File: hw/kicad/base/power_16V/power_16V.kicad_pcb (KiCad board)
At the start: 2 copper layers, 45 x 45 mm, 33 parts, among them J1 USB_B_Micro, J3 TOP, J4 BUTTOM, U1 LM2596S-5, U2 LM1117MP-3.3, U3 CP2104

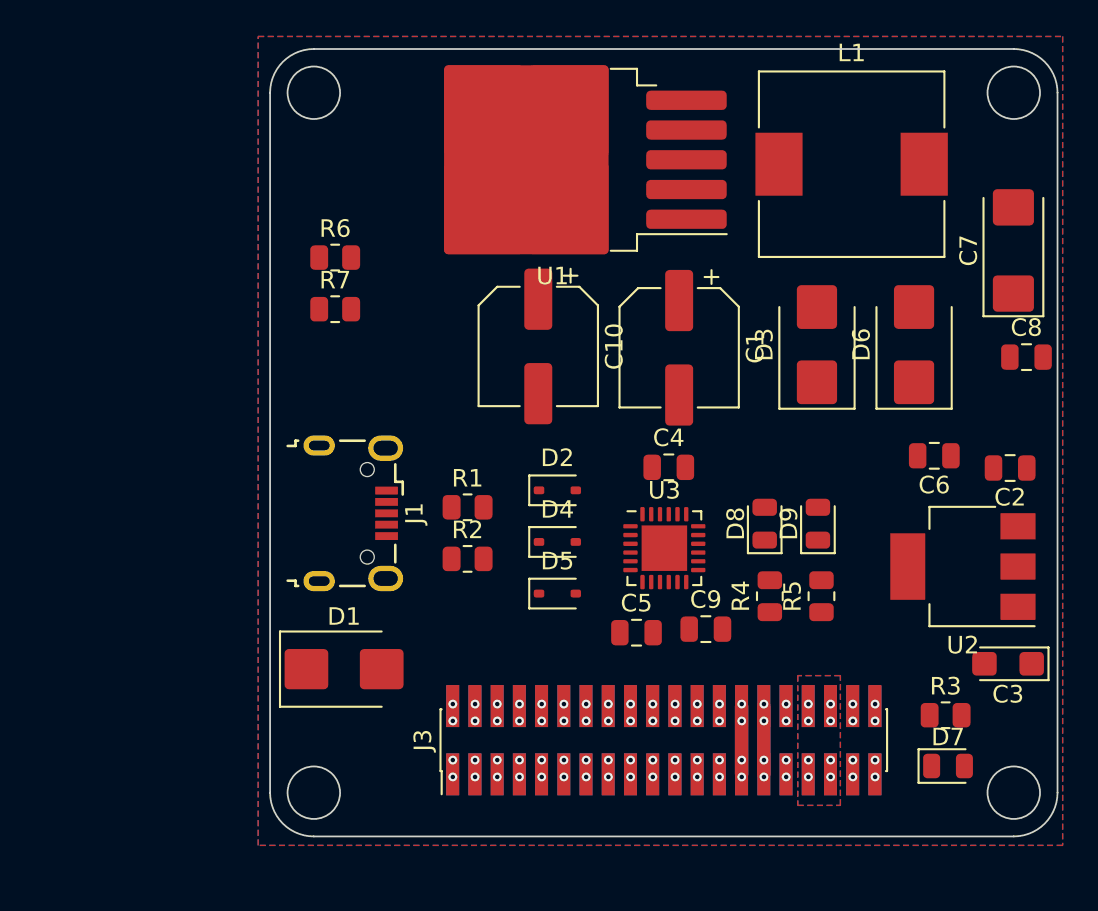
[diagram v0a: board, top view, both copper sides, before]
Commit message: 尽力改成40mmx40mm
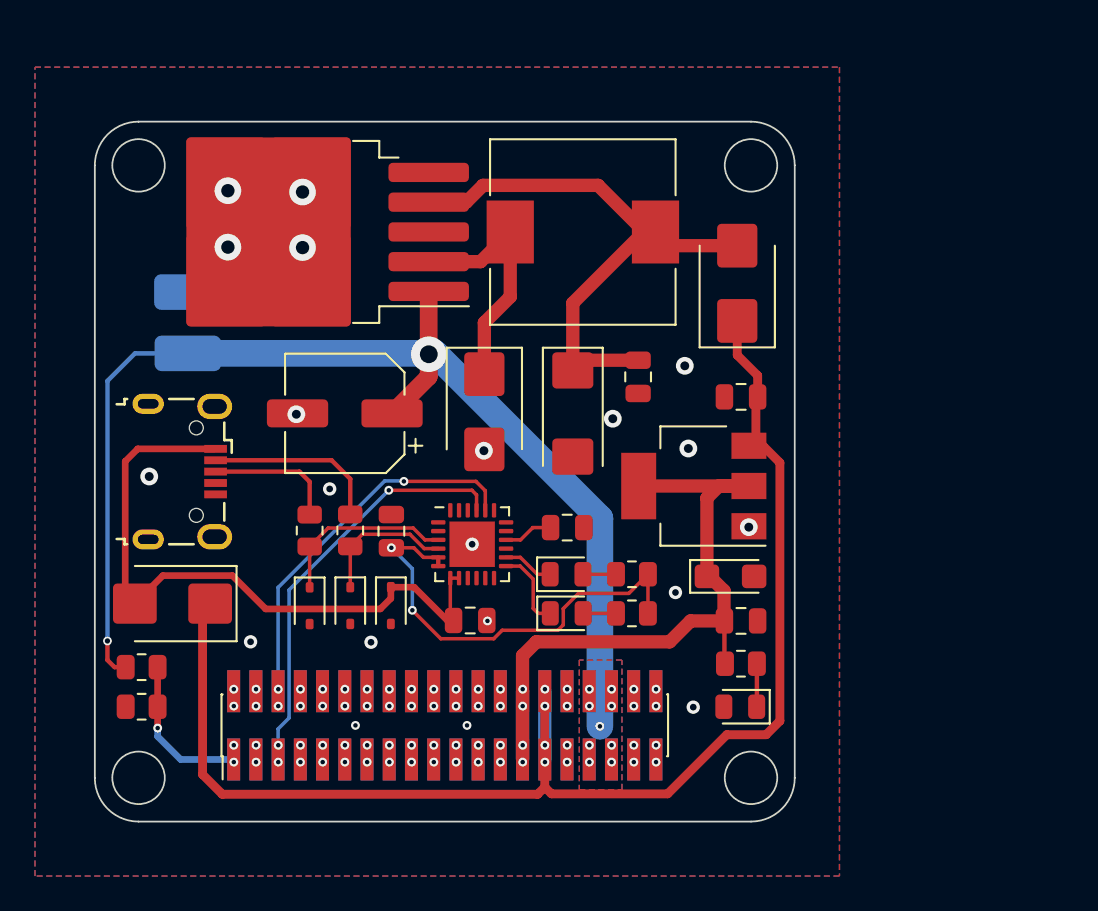
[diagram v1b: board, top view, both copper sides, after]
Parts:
- removed C10: 220uF, Capacitor_SMD:CP_Elec_6.3x7.7
- added ?: , , B.Cu at (46.0, 46.6)
- added ?: , , B.Cu at (46.0, 50.1)
- C1: value 220uF -> 100uF
- moved C7 26.8 mm to (68.0, 53.6), turned to -90 degrees
- moved R6 25.9 mm to (43.4, 68.0)
- moved R7 25.3 mm to (43.4, 70.3), turned to 180 degrees
- moved C8 22.2 mm to (71.8, 51.5), turned to -90 degrees
- moved C1 19.5 mm to (55.0, 53.5), turned to 180 degrees
- moved D3 19.4 mm to (63.0, 53.5), turned to -90 degrees
- moved C9 18.8 mm to (57.7, 60.3), turned to -90 degrees
- moved C3 16.6 mm to (77.0, 62.9), turned to 0 degrees
- moved U2 16.1 mm to (74.9, 57.7)
- moved C2 15.9 mm to (77.6, 52.6)
- moved L1 15.8 mm to (68.6, 43.2)
- moved U1 15.3 mm to (52.1, 43.2)
- moved D9 14.7 mm to (67.7, 62.7), turned to 0 degrees
- moved C6 14.5 mm to (77.6, 65.4), turned to 0 degrees
- moved D5 14.2 mm to (53.0, 64.5), turned to -90 degrees
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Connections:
- D7 pad 2: +3.3V -> GND
- J3 pad 10: /UART3_Tx -> /I2C_CLK
- J3 pad 11: /I2C_SDA -> /SPI_CS
- J3 pad 12: /I2C_CLK -> /SPI_CLK
- J3 pad 13: /SPI_CS -> /SPI_MOSI
- J3 pad 14: /SPI_CLK -> /SPI_MISO
- J3 pad 15: /SPI_MOSI -> /GPIO_1
- J3 pad 16: /SPI_MISO -> /GPIO_2
- J3 pad 17: /GPIO_1 -> /GPIO_3
- J3 pad 18: /GPIO_2 -> /GPIO_4
- J3 pad 19: /GPIO_3 -> /GPIO_5
- J3 pad 20: /GPIO_4 -> /GPIO_6
- J3 pad 21: /GPIO_5 -> /GPIO_7
- J3 pad 22: /GPIO_6 -> /GPIO_8
- J3 pad 23: /GPIO_7 -> /GPIO_9
- J3 pad 24: /GPIO_8 -> /GPIO_10
- J3 pad 25: /GPIO_9 -> /GPIO_11
- J3 pad 26: /GPIO_10 -> /GPIO_12
- J3 pad 9: /UART3_Rx -> /I2C_SDA
- J4 pad 10: /UART3_Rx -> /I2C_SDA
- J4 pad 11: /I2C_CLK -> /SPI_CLK
- J4 pad 12: /I2C_SDA -> /SPI_CS
- J4 pad 13: /SPI_CLK -> /SPI_MISO
- J4 pad 14: /SPI_CS -> /SPI_MOSI
- J4 pad 15: /SPI_MISO -> /GPIO_2
- J4 pad 16: /SPI_MOSI -> /GPIO_1
- J4 pad 17: /GPIO_2 -> /GPIO_4
- J4 pad 18: /GPIO_1 -> /GPIO_3
- J4 pad 19: /GPIO_4 -> /GPIO_6
- J4 pad 20: /GPIO_3 -> /GPIO_5
- J4 pad 21: /GPIO_6 -> /GPIO_8
- J4 pad 22: /GPIO_5 -> /GPIO_7
- J4 pad 23: /GPIO_8 -> /GPIO_10
- J4 pad 24: /GPIO_7 -> /GPIO_9
- J4 pad 25: /GPIO_10 -> /GPIO_12
- J4 pad 26: /GPIO_9 -> /GPIO_11
- J4 pad 9: /UART3_Tx -> /I2C_CLK
- R3 pad 1: GND -> +3.3V
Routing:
- net +5V: track 7.80 -> 79.6 mm
- net +BATT: track 0.00 -> 69.6 mm, vias 8 -> 11
- net Net-(D1-A): track 0.00 -> 38.2 mm
- net Net-(D6-A): track 0.00 -> 33.7 mm
- net +3.3V: track 7.80 -> 41.2 mm
- net /VIO: track 0.00 -> 25.9 mm, vias 0 -> 2
- net /UART1_Rx: track 0.00 -> 24.0 mm, vias 2 -> 3
- net /UART1_Tx: track 0.00 -> 21.6 mm, vias 2 -> 3
- net Net-(D3-K): track 0.00 -> 14.1 mm
- net Net-(D5-K): track 0.00 -> 10.4 mm
- net Net-(J1-D-): track 0.00 -> 10.2 mm
- net /ADC_1: track 0.00 -> 8.85 mm, vias 2 -> 3
- net Net-(D4-K): track 0.00 -> 7.99 mm
- net Net-(J1-D+): track 0.00 -> 7.49 mm
- net Net-(D8-K): track 0.00 -> 4.63 mm
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- added copper zone on B.Cu, net +BATT
- added copper zone on F.Cu, net +BATT
- added copper zone on B.Cu, net GND
- added copper zone on F.Cu, net GND
- removed copper zone on B.Cu, net (none)
- removed copper zone on F.Cu, net (none)
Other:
- board size 45 x 45 mm -> 40 x 40 mm
- board text added: "Pindar v1.3 Type BASE power16v v1.2"

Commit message: Merge from normal
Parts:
- removed the ? at (46.0, 46.6)
- removed the ? at (46.0, 50.1)
- added ?: , , B.Cu at (54.3, 46.6)
- added ?: , , B.Cu at (54.3, 42.8)
- added C10: 220uF, Capacitor_SMD:CP_Elec_6.3x7.7, F.Cu at (66.0, 49.7)
- added C11: 0.1uF, Capacitor_SMD:C_0805_2012Metric, F.Cu at (58.1, 39.4)
- added C12: 0.1uF, Capacitor_SMD:C_0805_2012Metric, F.Cu at (54.4, 39.4)
- added U4: ACS712xLCTR-05B, Package_SO:SOIC-8_3.9x4.9mm_P1.27mm, F.Cu at (56.2, 44.6)
- C1: value 100uF -> 220uF
- R1, R2: footprint Resistor_SMD:R_0805_2012Metric -> Resistor_SMD:R_0603_1608Metric
- R4, R5: value 22 -> 100
- moved C7 27.0 mm to (92.9, 43.1), turned to 90 degrees
- moved R7 22.0 mm to (56.3, 52.5)
- moved R6 21.9 mm to (56.3, 50.4)
- moved C8 21.3 mm to (92.9, 48.9), turned to 0 degrees
- moved C1 19.5 mm to (74.1, 49.7), turned to -90 degrees
- moved D3 19.4 mm to (82.0, 49.6)
- moved C9 18.6 mm to (75.3, 66.1), turned to 180 degrees
- moved L1 16.5 mm to (84.6, 39.3)
- moved U1 15.9 mm to (67.5, 39.1)
- moved C6 15.7 mm to (92.7, 69.8)
- moved C3 15.6 mm to (92.1, 66.8)
- moved U2 15.5 mm to (90.0, 61.3)
- moved C2 15.4 mm to (92.7, 55.6)
- moved D7 13.3 mm to (82.4, 57.9), turned to 0 degrees
- moved J3 12.5 mm to (73.2, 72.2)
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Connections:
- net Net-(D6-A) renamed /DCDC_+5V
- D7 pad 2: GND -> +3.3V
- J3 pad 10: /I2C_CLK -> /UART3_Tx
- J3 pad 11: /SPI_CS -> /I2C_SDA
- J3 pad 12: /SPI_CLK -> /I2C_CLK
- J3 pad 13: /SPI_MOSI -> /SPI_CS
- J3 pad 14: /SPI_MISO -> /SPI_CLK
- J3 pad 15: /GPIO_1 -> /SPI_MOSI
- J3 pad 16: /GPIO_2 -> /SPI_MISO
- J3 pad 17: /GPIO_3 -> /GPIO_1
- J3 pad 18: /GPIO_4 -> /GPIO_2
- J3 pad 19: /GPIO_5 -> /GPIO_3
- J3 pad 20: /GPIO_6 -> /GPIO_4
- J3 pad 21: /GPIO_7 -> /GPIO_5
- J3 pad 22: /GPIO_8 -> /GPIO_6
- J3 pad 23: /GPIO_9 -> /GPIO_7
- J3 pad 24: /GPIO_10 -> /GPIO_8
- J3 pad 25: /GPIO_11 -> /GPIO_9
- J3 pad 26: /GPIO_12 -> /GPIO_10
- J3 pad 9: /I2C_SDA -> /UART3_Rx
- J4 pad 10: /I2C_SDA -> /UART3_Rx
- J4 pad 11: /SPI_CLK -> /I2C_CLK
- J4 pad 12: /SPI_CS -> /I2C_SDA
- J4 pad 13: /SPI_MISO -> /SPI_CLK
- J4 pad 14: /SPI_MOSI -> /SPI_CS
- J4 pad 15: /GPIO_2 -> /SPI_MISO
- J4 pad 16: /GPIO_1 -> /SPI_MOSI
- J4 pad 17: /GPIO_4 -> /GPIO_2
- J4 pad 18: /GPIO_3 -> /GPIO_1
- J4 pad 19: /GPIO_6 -> /GPIO_4
- J4 pad 20: /GPIO_5 -> /GPIO_3
- J4 pad 21: /GPIO_8 -> /GPIO_6
- J4 pad 22: /GPIO_7 -> /GPIO_5
- J4 pad 23: /GPIO_10 -> /GPIO_8
- J4 pad 24: /GPIO_9 -> /GPIO_7
- J4 pad 25: /GPIO_12 -> /GPIO_10
- J4 pad 26: /GPIO_11 -> /GPIO_9
- J4 pad 9: /I2C_CLK -> /UART3_Tx
- R3 pad 1: +3.3V -> GND
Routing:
- net /ADC_2: track 0.00 -> 43.7 mm
- net /DCDC_+5V: track 33.7 -> 69.0 mm, vias 0 -> 2
- net /ADC_1: track 8.85 -> 29.4 mm, vias 3 -> 2
- net +BATT: track 69.6 -> 54.2 mm, vias 11 -> 12
- net +3.3V: track 41.2 -> 49.4 mm
- net Net-(J1-D-): track 10.2 -> 3.43 mm
- net /VIO: track 25.9 -> 20.0 mm
- net Net-(D4-K): track 7.99 -> 13.2 mm
- net Net-(U3-VPP): track 2.83 -> 7.27 mm
- net Net-(J1-D+): track 7.49 -> 3.50 mm
- net Net-(D1-A): track 38.2 -> 41.6 mm, vias 0 -> 4
- net Net-(U4-FILTER): track 0.00 -> 2.91 mm
- net +5V: track 79.6 -> 82.5 mm, vias 4 -> 8
- net Net-(D8-K): track 4.63 -> 3.14 mm
- net /UART1_Rx: track 24.0 -> 25.2 mm
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- added copper zone on B.Cu, net /+BATT_IN
- added copper zone on F.Cu, net /+BATT_IN
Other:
- board size 40 x 40 mm -> 45 x 45 mm
- board text added: "Pindar v1.2 (Base) power16v v1.2"
- board text removed: "Pindar v1.3 Type BASE power16v v1.2"
